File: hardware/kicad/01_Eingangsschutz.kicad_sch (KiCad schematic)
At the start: 4 parts, among them K101 G6S-2F DC5 - C16707, Q111 DMN2056U-7

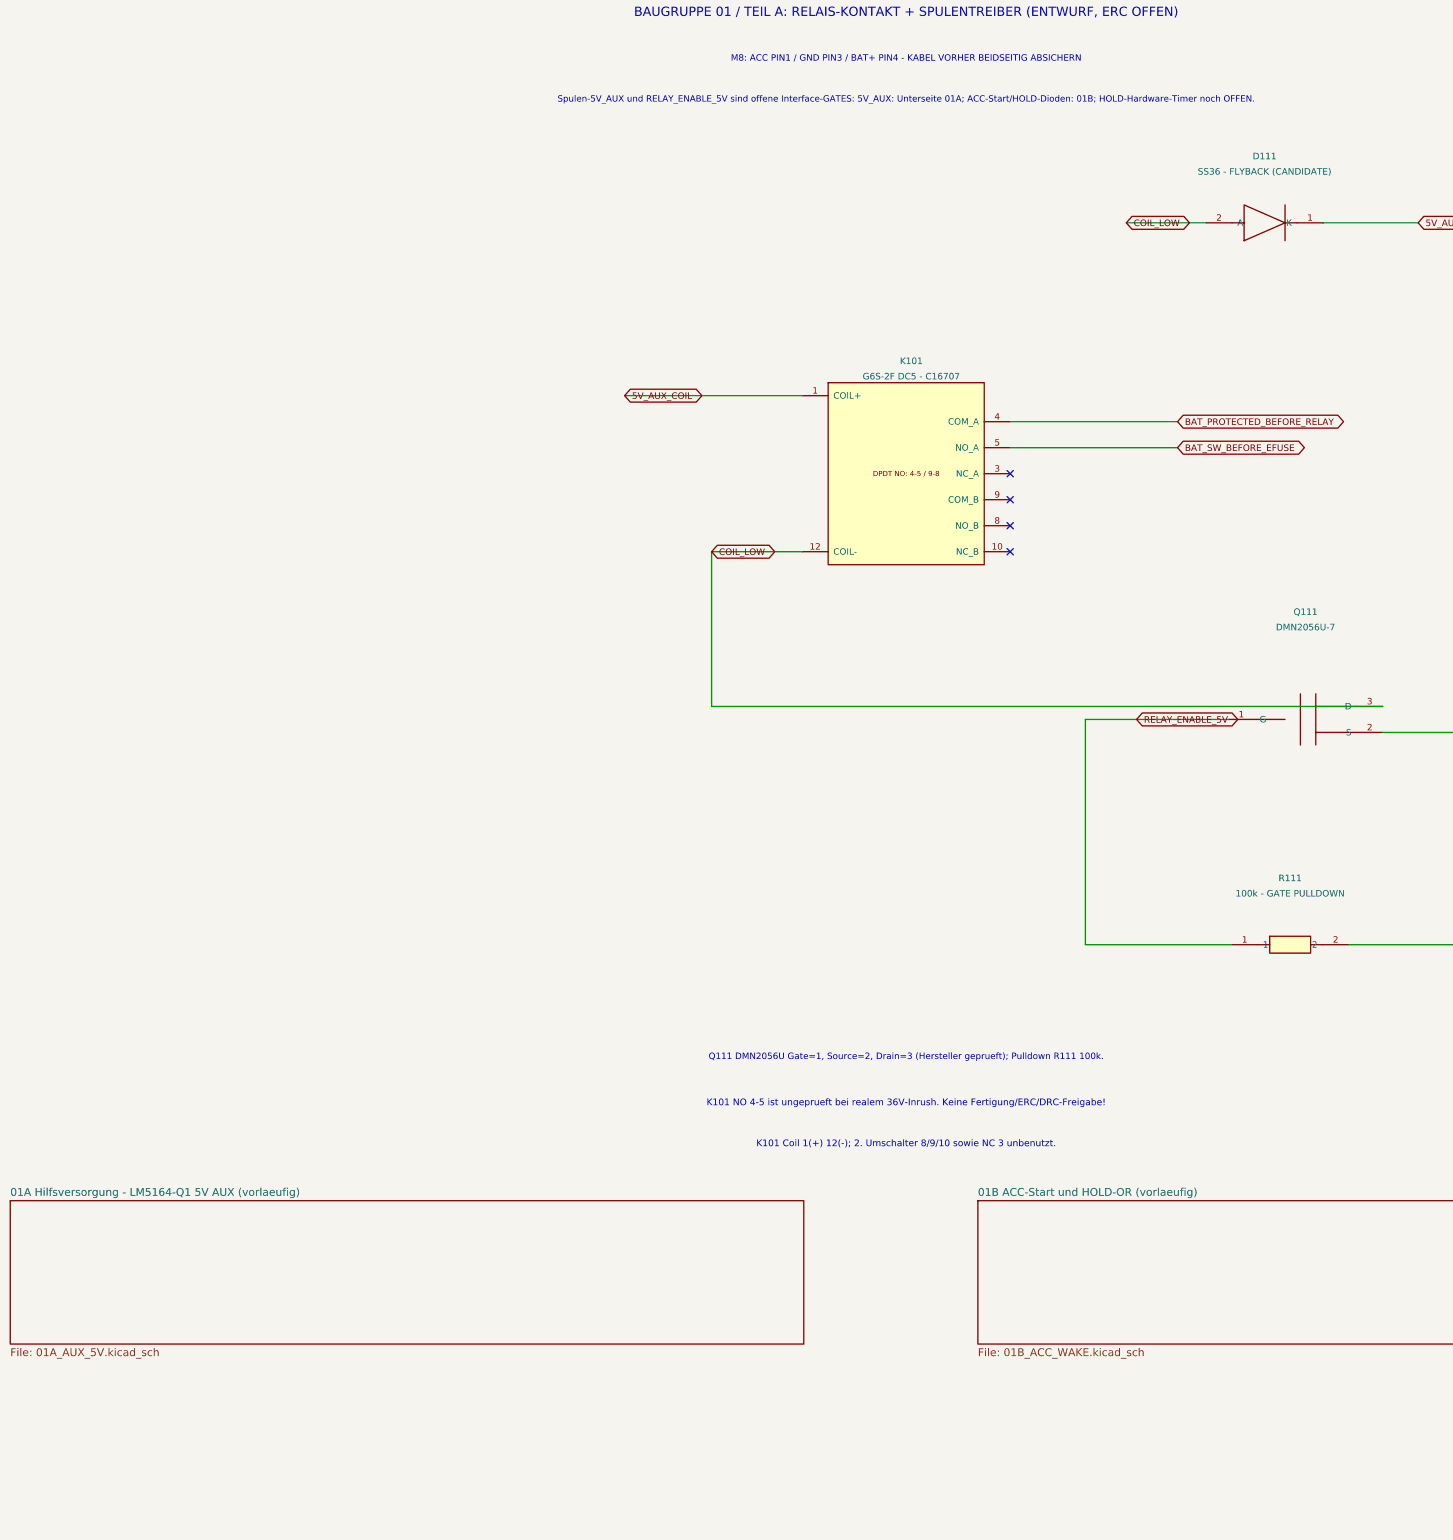
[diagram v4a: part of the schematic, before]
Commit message: hardware(kicad): add 01C TLC555-Q1 max relay hold timer and gated MCU hold signal
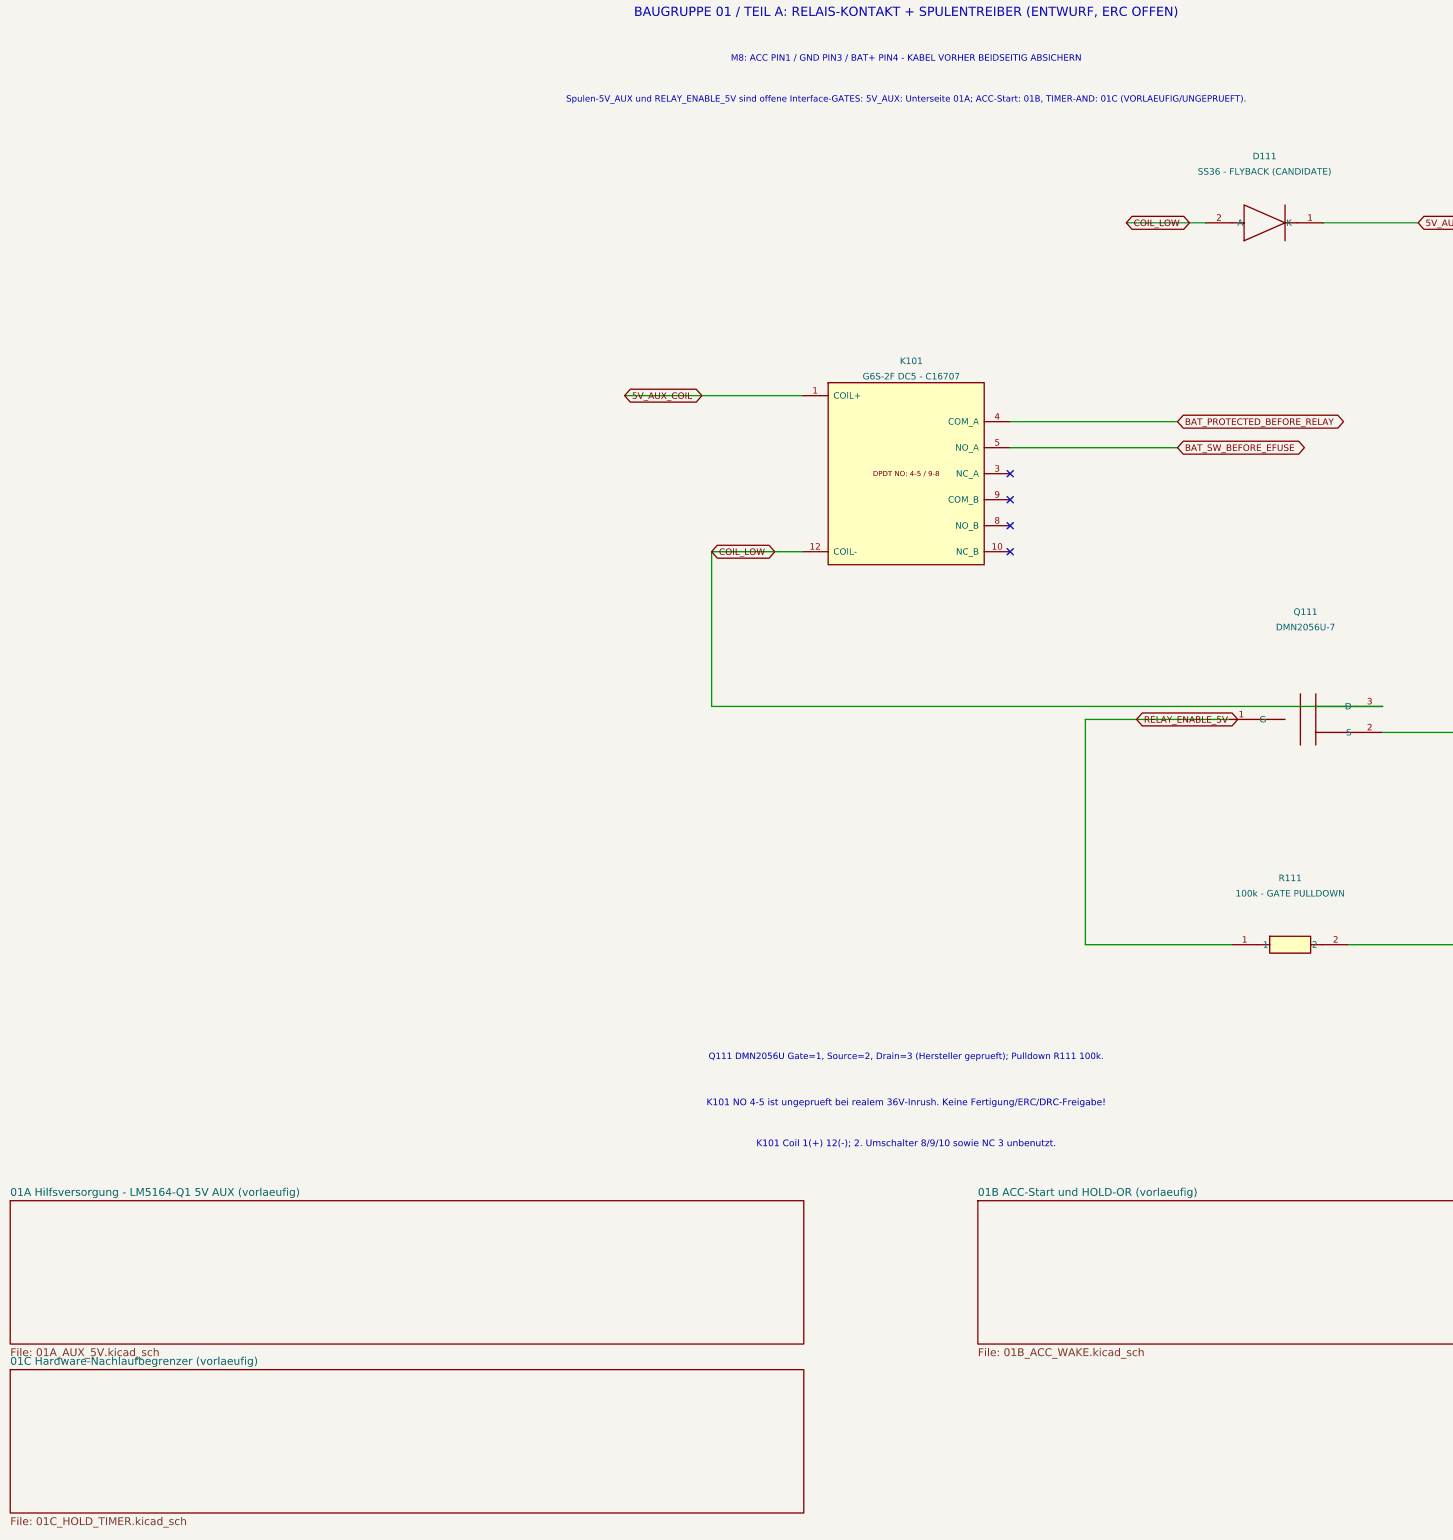
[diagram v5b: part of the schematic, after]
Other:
- added sheet 01C Hardware-Nachlaufbegrenzer (vorlaeufig) (01C_HOLD_TIMER.kicad_sch)
- note added: "Spulen-5V_AUX und RELAY_ENABLE_5V sind offene Interface-GATES: 5V_AUX: Unterseite 01A; ACC-Start: 01B, TIMER-AND: 01C (VORLAEUFIG/UNGEPRUEFT)."
- note removed: "Spulen-5V_AUX und RELAY_ENABLE_5V sind offene Interface-GATES: 5V_AUX: Unterseite 01A; ACC-Start/HOLD-Dioden: 01B; HOLD-Hardware-Timer noch OFFEN."
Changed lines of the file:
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@@
 (kicad_sch (version 20250114) (generator "eeschema")
- (paper "A3")
+ (paper "A2")
  (title_block (title "TripTracer V1 - ACC/BAT+ Eingangsschutz und Relais") (date "2026-10-13") (rev "a1 / RELAIS-TEILENTWURF - NICHT ERC-GEPRUEFT"))
  (symbol (lib_id "TripTracer_V1:G6S_2F_DC5") (at 200 115 0) (unit 1) (exclude_from_sim no) (in_bom yes) (on_board yes) (dnp no)
@@
 (text "BAUGRUPPE 01 / TEIL A: RELAIS-KONTAKT + SPULENTREIBER (ENTWURF, ERC OFFEN)" (at 200 25 0) (effects (font (size 1.8 1.8))))
 (text "M8: ACC PIN1 / GND PIN3 / BAT+ PIN4 - KABEL VORHER BEIDSEITIG ABSICHERN" (at 200 34 0) (effects (font (size 1.25 1.25))))
-(text "Spulen-5V_AUX und RELAY_ENABLE_5V sind offene Interface-GATES: 5V_AUX: Unterseite 01A; ACC-Start/HOLD-Dioden: 01B; HOLD-Hardware-Timer noch OFFEN." (at 200 42 0) (effects (font (size 1.23 1.23))))
+(text "Spulen-5V_AUX und RELAY_ENABLE_5V sind offene Interface-GATES: 5V_AUX: Unterseite 01A; ACC-Start: 01B, TIMER-AND: 01C (VORLAEUFIG/UNGEPRUEFT)." (at 200 42 0) (effects (font (size 1.23 1.23))))
 (text "Q111 DMN2056U Gate=1, Source=2, Drain=3 (Hersteller geprueft); Pulldown R111 100k." (at 200 229 0) (effects (font (size 1.25 1.25))))
 (text "K101 NO 4-5 ist ungeprueft bei realem 36V-Inrush. Keine Fertigung/ERC/DRC-Freigabe!" (at 200 238 0) (effects (font (size 1.3 1.3))))
@@
  (instances (project "TripTracer_V1" (path "/a26d9b0c-7f10-4e5a-a65f-000000000064/a26d9b0c-7f10-4e5a-a65f-000000000065" (page "2.2"))))
 )
+(sheet (at 25 290) (size 155 28) (exclude_from_sim no) (in_bom yes) (on_board yes) (dnp no)
+(stroke (width 0) (type solid)) (fill (color 0 0 0 0))
+(property "Sheetname" "01C Hardware-Nachlaufbegrenzer (vorlaeufig)" (at 25 289.24 0) (effects (font (size 1.524 1.524)) (justify left bottom)))
+(property "Sheetfile" "01C_HOLD_TIMER.kicad_sch" (at 25 318.76 0) (effects (font (size 1.524 1.524)) (justify left top)))
+(instances (project "TripTracer_V1" (path "/a26d9b0c-7f10-4e5a-a65f-000000000064/a26d9b0c-7f10-4e5a-a65f-000000000065" (page "2.3"))))
+)
  (sheet_instances (path "/" (page "2")))

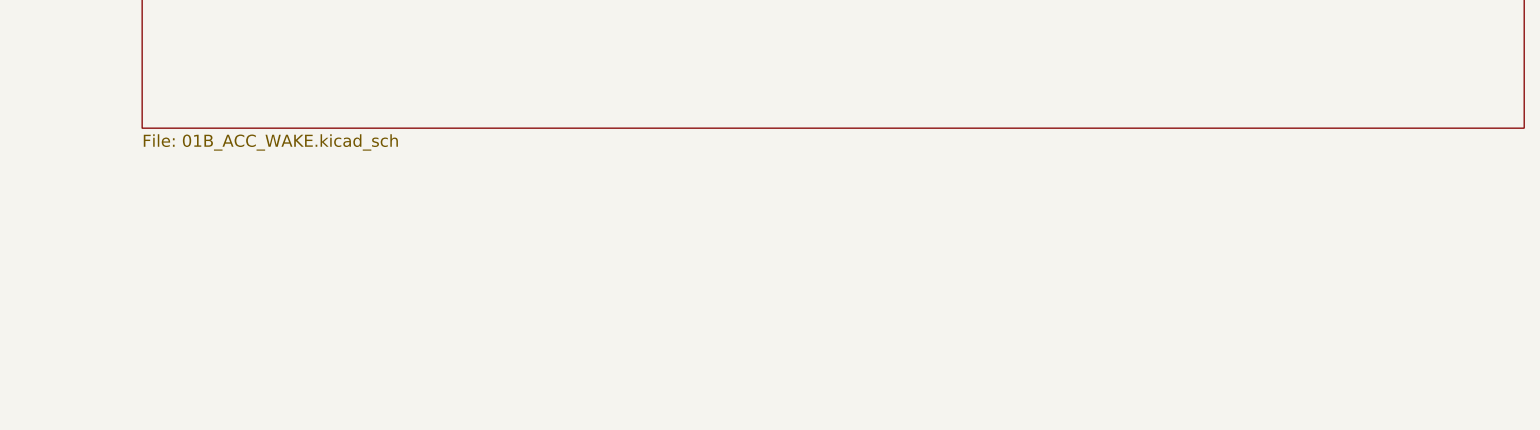
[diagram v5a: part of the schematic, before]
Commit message: hardware: prepare 36V-compatible TPS26631 protection sheet and document dual battery path safety gates
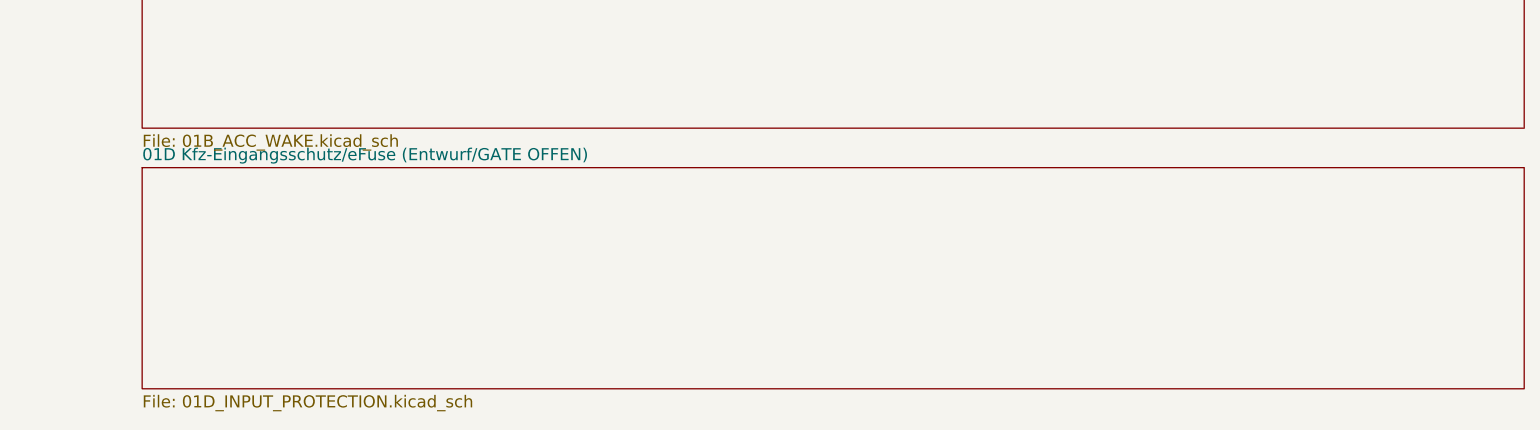
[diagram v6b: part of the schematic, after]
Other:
- added sheet 01D Kfz-Eingangsschutz/eFuse (Entwurf/GATE OFFEN) (01D_INPUT_PROTECTION.kicad_sch)
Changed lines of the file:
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@@
 (instances (project "TripTracer_V1" (path "/a26d9b0c-7f10-4e5a-a65f-000000000064/a26d9b0c-7f10-4e5a-a65f-000000000065" (page "2.3"))))
+)
+(sheet (at 214 290) (size 175 28) (exclude_from_sim no) (in_bom yes) (on_board yes) (dnp no)
+ (stroke (width 0) (type solid)) (fill (color 0 0 0 0))
+ (property "Sheetname" "01D Kfz-Eingangsschutz/eFuse (Entwurf/GATE OFFEN)" (at 214 289.24 0) (effects (font (size 1.524 1.524)) (justify left bottom)))
+ (property "Sheetfile" "01D_INPUT_PROTECTION.kicad_sch" (at 214 318.76 0) (effects (font (size 1.524 1.524)) (justify left top)))
+ (instances (project "TripTracer_V1" (path "/a26d9b0c-7f10-4e5a-a65f-000000000064/a26d9b0c-7f10-4e5a-a65f-000000000065" (page "2.4"))))
 )
  (sheet_instances (path "/" (page "2")))

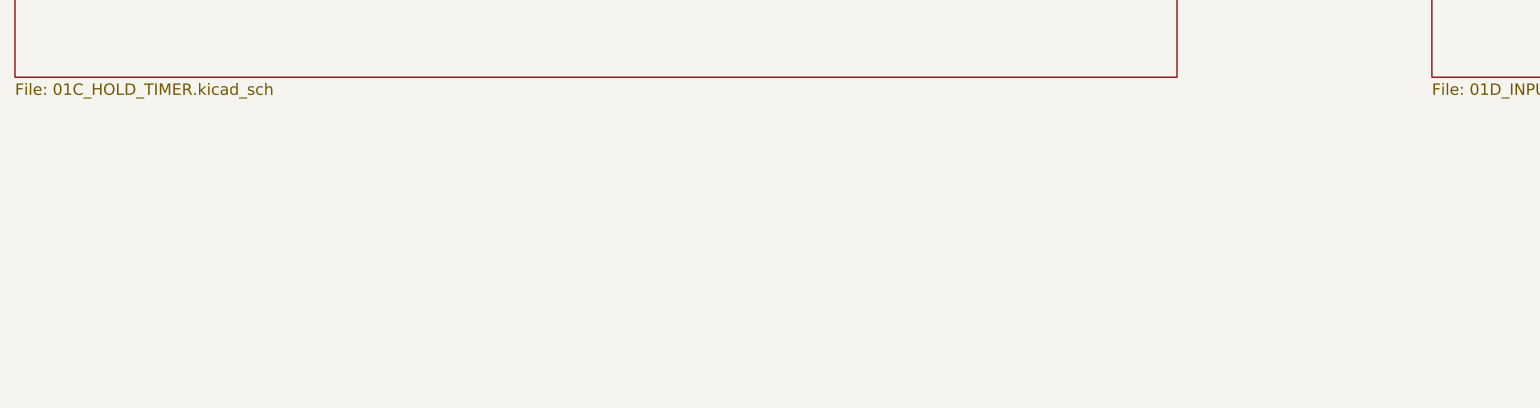
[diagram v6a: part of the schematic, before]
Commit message: hardware(kicad): link 01E latch into unified V1 hierarchy
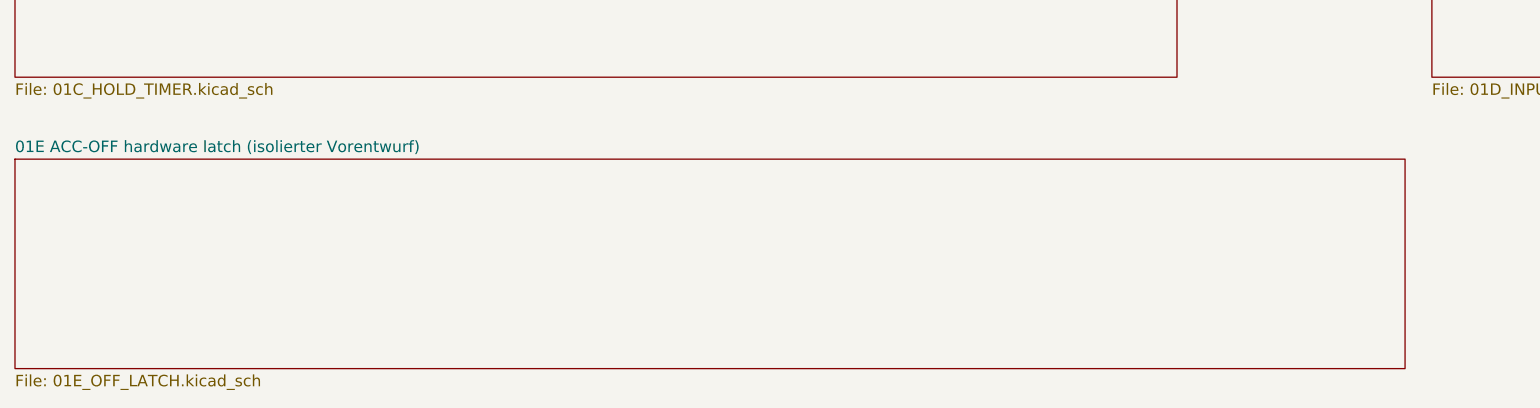
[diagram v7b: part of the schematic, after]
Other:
- added sheet 01E ACC-OFF hardware latch (isolierter Vorentwurf) (01E_OFF_LATCH.kicad_sch)
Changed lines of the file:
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@@
  (instances (project "TripTracer_V1" (path "/a26d9b0c-7f10-4e5a-a65f-000000000064/a26d9b0c-7f10-4e5a-a65f-000000000065" (page "2.4"))))
 )
- (sheet_instances (path "/" (page "2")))
+ (sheet (at 25 328.93) (size 185.42 27.94) (exclude_from_sim no) (in_bom yes) (on_board yes) (dnp no)
+ (stroke (width 0) (type solid)) (fill (color 0 0 0 0))
+ (property "Sheetname" "01E ACC-OFF hardware latch (isolierter Vorentwurf)" (at 25 328.17 0) (effects (font (size 1.524 1.524)) (justify left bottom)))
+ (property "Sheetfile" "01E_OFF_LATCH.kicad_sch" (at 25 357.63 0) (effects (font (size 1.524 1.524)) (justify left top)))
+ (instances (project "TripTracer_V1" (path "/a26d9b0c-7f10-4e5a-a65f-000000000064/a26d9b0c-7f10-4e5a-a65f-000000000065" (page "2.5"))))
+)
+(sheet_instances (path "/" (page "2")))
  (embedded_fonts no)
 )

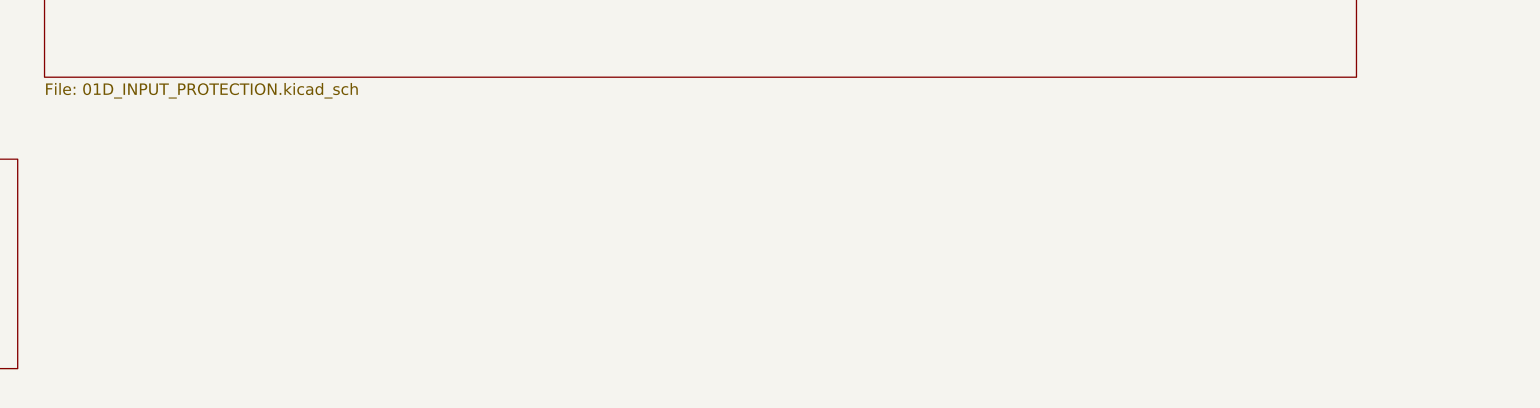
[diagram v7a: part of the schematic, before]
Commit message: hardware(kicad): link cheap autonomous RC shutdown prototype as sheet 01F
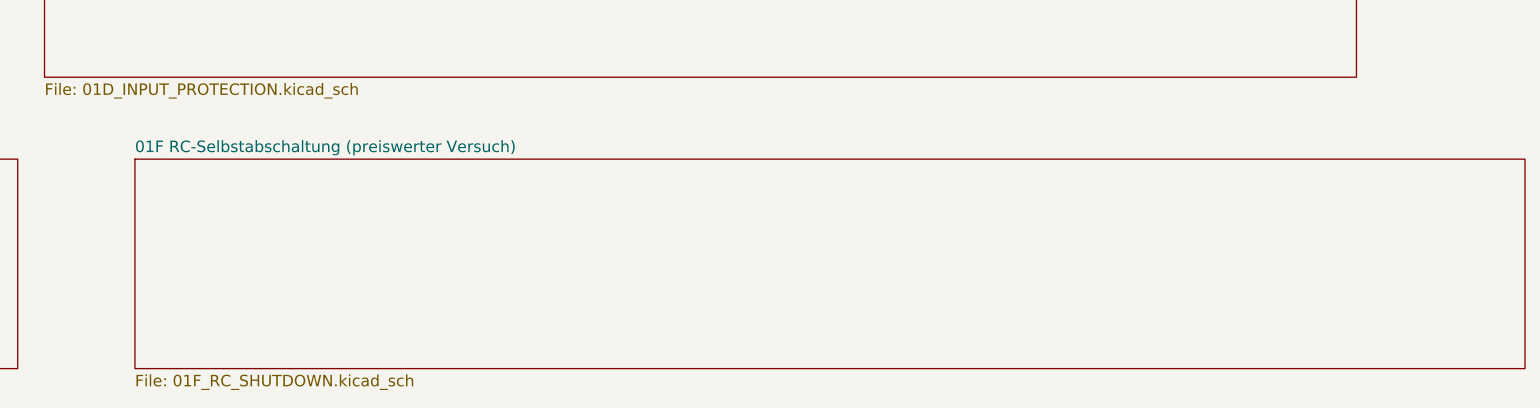
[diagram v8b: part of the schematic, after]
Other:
- added sheet 01F RC-Selbstabschaltung (preiswerter Versuch) (01F_RC_SHUTDOWN.kicad_sch)
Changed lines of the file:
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@@
  (instances (project "TripTracer_V1" (path "/a26d9b0c-7f10-4e5a-a65f-000000000064/a26d9b0c-7f10-4e5a-a65f-000000000065" (page "2.5"))))
+)
+(sheet (at 226.06 328.93) (size 185.42 27.94) (exclude_from_sim no) (in_bom yes) (on_board yes) (dnp no)
+ (stroke (width 0) (type solid)) (fill (color 0 0 0 0))
+ (property "Sheetname" "01F RC-Selbstabschaltung (preiswerter Versuch)" (at 226.06 328.17 0) (effects (font (size 1.524 1.524)) (justify left bottom)))
+ (property "Sheetfile" "01F_RC_SHUTDOWN.kicad_sch" (at 226.06 357.63 0) (effects (font (size 1.524 1.524)) (justify left top)))
+ (instances (project "TripTracer_V1" (path "/a26d9b0c-7f10-4e5a-a65f-000000000064/a26d9b0c-7f10-4e5a-a65f-000000000065" (page "2.6"))))
 )
 (sheet_instances (path "/" (page "2")))
